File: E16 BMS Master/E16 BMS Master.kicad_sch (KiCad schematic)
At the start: 31 parts, among them J1 Analog, Q1 IRLML2502, Q2 IRLML2060, Q3 IRLML2060, U1 PDQE20-Ds_Self

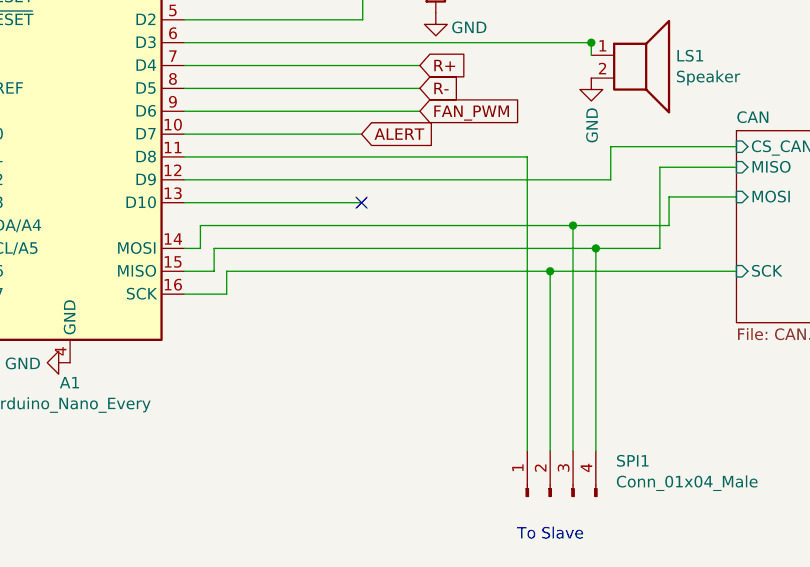
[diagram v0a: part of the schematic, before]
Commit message: added 5k pullup for MISO
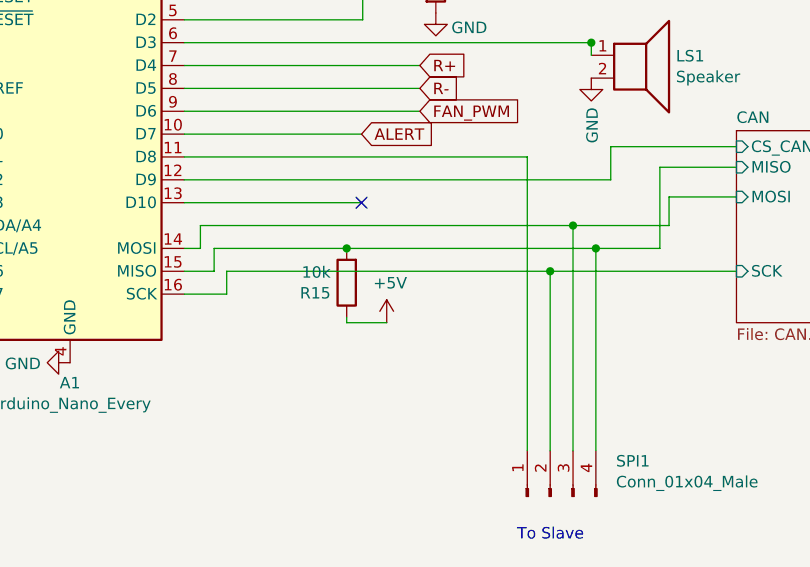
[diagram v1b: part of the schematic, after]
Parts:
- added R15: 10k, Resistor_SMD:R_1206_3216Metric_Pad1.30x1.75mm_HandSolder, symbol Device:R
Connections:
- net +5V: now also R15.1
- net CAN/MISO: now also R15.2
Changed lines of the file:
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@@
   (junction (at 39.751 48.514) (diameter 0) (color 0 0 0 0)
+  )
+  (junction (at 146.685 114.3) (diameter 0) (color 0 0 0 0)
   )
   (junction (at 29.337 30.226) (diameter 0) (color 0 0 0 0)
@@
     (stroke (width 0) (type default))
   )
+  (wire (pts (xy 146.685 122.555) (xy 146.685 121.92))
+    (stroke (width 0) (type default))
+  )
   (wire (pts (xy 109.22 35.687) (xy 109.22 36.322))
     (stroke (width 0) (type default))
@@
     (stroke (width 0) (type default))
   )
+  (wire (pts (xy 146.685 122.555) (xy 151.13 122.555))
+    (stroke (width 0) (type default))
+  )
   (wire (pts (xy 133.35 116.84) (xy 169.291 116.84))
     (stroke (width 0) (type default))
@@
   )
   (wire (pts (xy 210.82 46.482) (xy 217.297 46.482))
+    (stroke (width 0) (type default))
+  )
+  (wire (pts (xy 146.685 114.3) (xy 174.371 114.3))
     (stroke (width 0) (type default))
   )
@@
     (stroke (width 0) (type default))
   )
-  (wire (pts (xy 131.953 114.3) (xy 174.371 114.3))
+  (wire (pts (xy 131.953 114.3) (xy 146.685 114.3))
     (stroke (width 0) (type default))
   )
@@
         )
       )
+    )
+  )
+  (symbol (lib_id "Device:R") (at 146.685 118.11 180) (unit 1)
+    (in_bom yes) (on_board yes) (dnp no)
+    (property "Reference" "R15" (at 144.907 119.2784 0)
+      (effects (font (size 1.27 1.27)) (justify left))
+    )
+    (property "Value" "10k" (at 144.907 116.967 0)
+      (effects (font (size 1.27 1.27)) (justify left))
+    )
+    (property "Footprint" "Resistor_SMD:R_1206_3216Metric_Pad1.30x1.75mm_HandSolder" (at 148.463 118.11 90)
+      (effects (font (size 1.27 1.27)) hide)
+    )
+    (property "Datasheet" "~" (at 146.685 118.11 0)
+      (effects (font (size 1.27 1.27)) hide)
+    )
+    (pin "1")
+    (pin "2")
+    (instances
+      (project "E16 BMS Master"
+        (path "/187dc891-fba6-4fa1-ad68-fe8f7270f1a2"
+          (reference "R15") (unit 1)
+        )
+      )
+    )
+  )
+  (symbol (lib_id "power:+5V") (at 151.13 122.555 0) (unit 1)
+    (in_bom yes) (on_board yes) (dnp no)
+    (property "Reference" "#PWR017" (at 151.13 126.365 0)
+      (effects (font (size 1.27 1.27)) hide)
+    )
+    (property "Value" "+5V" (at 151.511 118.1608 0)
+      (effects (font (size 1.27 1.27)))
+    )
+    (property "Footprint" "" (at 151.13 122.555 0)
+      (effects (font (size 1.27 1.27)) hide)
+    )
+    (property "Datasheet" "" (at 151.13 122.555 0)
+      (effects (font (size 1.27 1.27)) hide)
+    )
+    (pin "1")
+    (instances
+      (project "E16 BMS Master"
+        (path "/187dc891-fba6-4fa1-ad68-fe8f7270f1a2"
+          (reference "#PWR017") (unit 1)
+        )
+      )
